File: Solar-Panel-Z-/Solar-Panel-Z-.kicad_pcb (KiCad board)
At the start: 6 copper layers, 48.4 x 48.4 mm, 73 parts, among them J1 FFC2B28-10-G, J2 U.FL-R-SMT-1, Q1 IRLML2803, U1 Value, U2 TSL2561, U3 NDS8434, U4 ATB2012-50011-T000

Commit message: Exported Gerbers
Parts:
- added H3: MountingHole, MountingHole:MountingHole_2.2mm_M2_DIN965, F.Cu at (84.0, 55.5)
- added H4: MountingHole, MountingHole:MountingHole_2.2mm_M2_DIN965, F.Cu at (84.0, 73.9)
- added H5: MountingHole, MountingHole:MountingHole_2.2mm_M2_DIN965, F.Cu at (123.8, 73.9)
- added H6: MountingHole, MountingHole:MountingHole_2.2mm_M2_DIN965, F.Cu at (123.8, 55.5)
- moved U2 0.97 mm to (112.4, 60.5)
- moved JP2 0.43 mm to (116.4, 53.7)
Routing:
- net /coil: track 13587.3 -> 13524.7 mm
- net GND: track 10.4 -> 9.34 mm, vias 1 -> 4
- net SDA1: track 30.1 -> 29.1 mm
- net SCL1: track 27.4 -> 26.4 mm
- net Net-(R1-Pad1): track 4.32 -> 3.37 mm
- net +3V3: track 59.0 -> 59.9 mm
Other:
- outline, holes or cut-outs redrawn

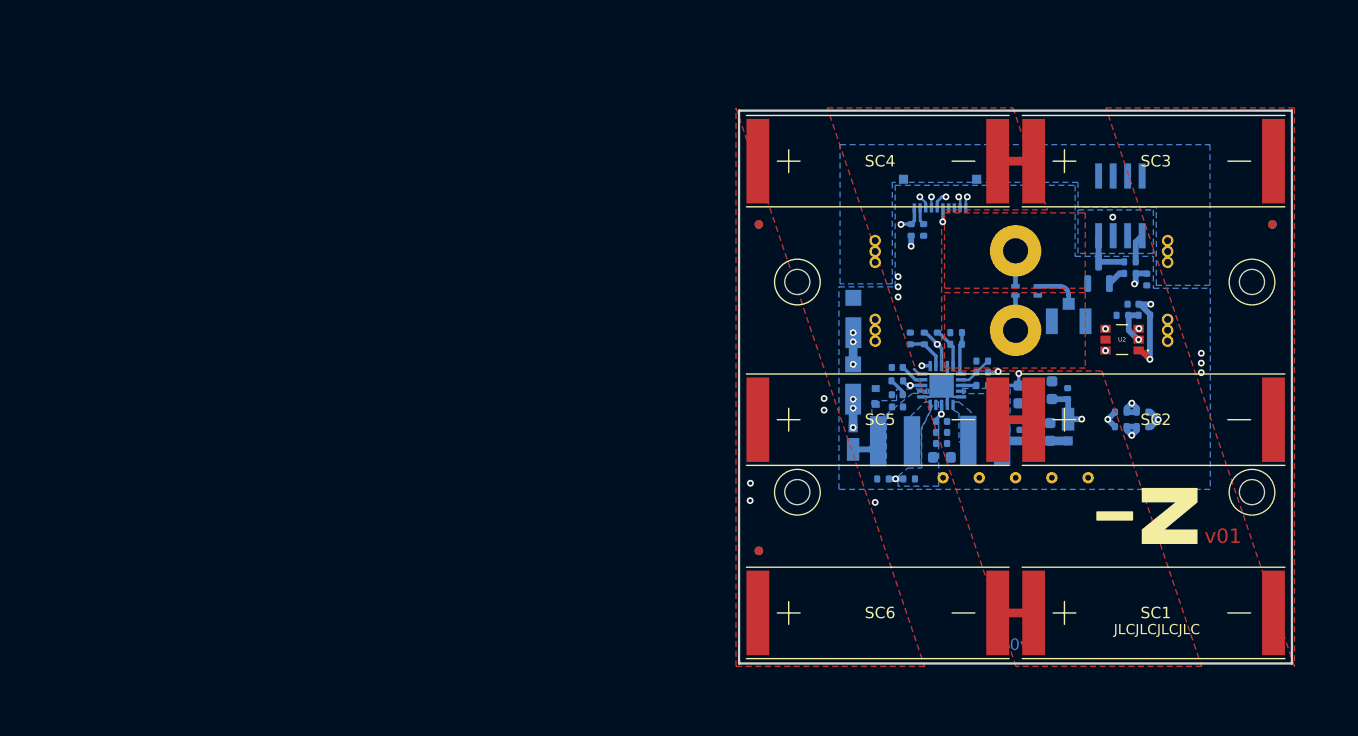
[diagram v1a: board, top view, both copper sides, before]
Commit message: Correct positions for everything except coils
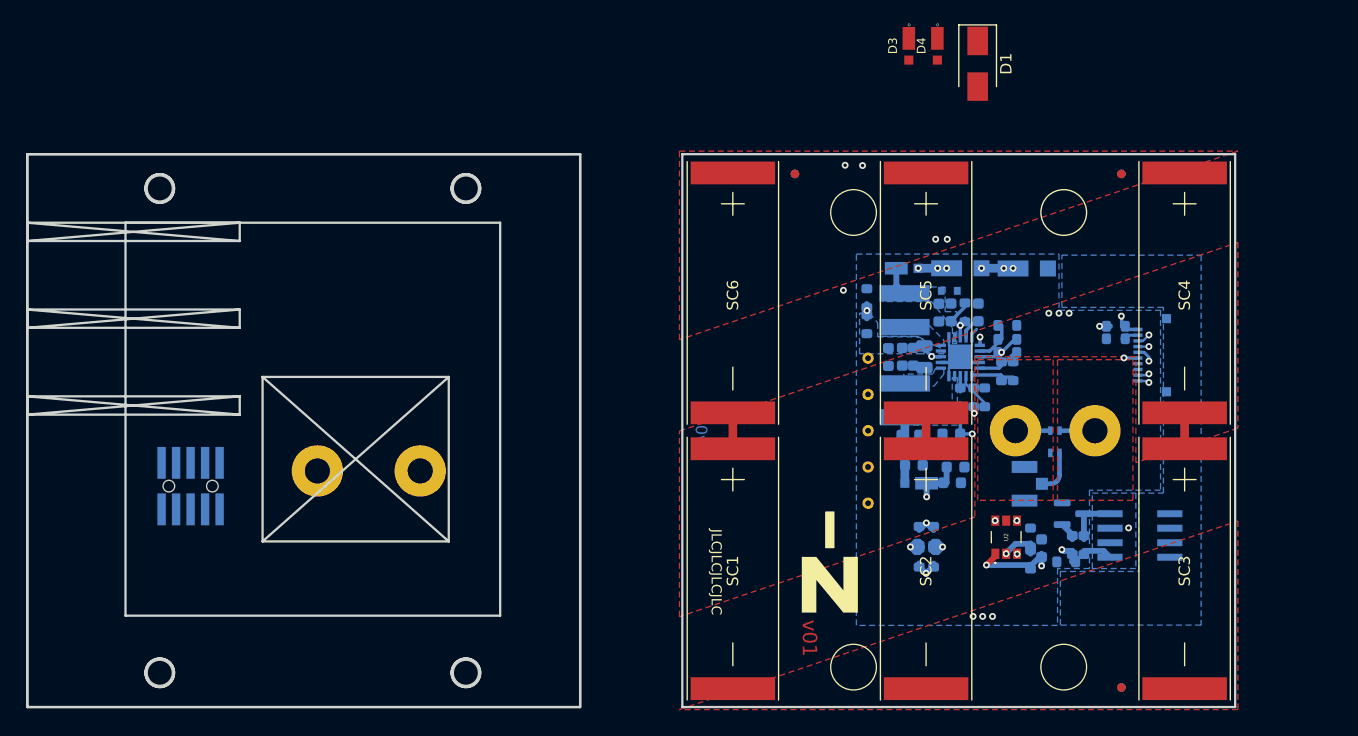
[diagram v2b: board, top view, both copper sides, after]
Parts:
- removed JP1, JP2: Jumper, solarpanels:Burn-Wire-Rotated
- added ?: , , F.Cu at (51.0, 72.0)
- added ?: , , F.Cu at (42.0, 72.0)
- added D1: SZ1SMA5918, Diode_SMD:D_SMA, F.Cu at (99.8, 36.4)
- added D3: MSS1P4-M3_89A, solarpanels:MICROSMP, F.Cu at (93.8, 34.8)
- added D4: MSS1P4-M3_89A, solarpanels:MICROSMP, F.Cu at (96.3, 34.8)
- added J1: TODO, batteryboard:FTS-105-XX-YY-DV-A, B.Cu at (30.9, 73.3)
- C1: value 1.0uF -> 1uF; footprint Capacitor_SMD:C_0402_1005Metric -> Capacitor_SMD:C_0603_1608Metric
- C10, C2, C3, C4, C9: footprint Capacitor_SMD:C_0402_1005Metric -> Capacitor_SMD:C_0603_1608Metric
- C11: renamed from C13; footprint Capacitor_SMD:C_0402_1005Metric -> Capacitor_SMD:C_0603_1608Metric
- C5: value 0.1uF -> 100uF; footprint Capacitor_SMD:C_0402_1005Metric -> Capacitor_SMD:C_0805_2012Metric
- C6: value 100uF -> 1uF
- C7: value 22uF -> 4.7uF; footprint Capacitor_SMD:C_0402_1005Metric -> Capacitor_SMD:C_0603_1608Metric
- C8: value 4.7uF -> 22uF; footprint Capacitor_SMD:C_0402_1005Metric -> Capacitor_SMD:C_0603_1608Metric
- R1, R10, R11, R12, R13, R14, R15, R16, R17, R18, R2, R5, R6, R7, R8, R9: footprint Resistor_SMD:R_0402_1005Metric -> Resistor_SMD:R_0603_1608Metric
- R19: renamed from R22; footprint Resistor_SMD:R_0402_1005Metric -> Resistor_SMD:R_0603_1608Metric
- R20: renamed from R3; footprint Resistor_SMD:R_0402_1005Metric -> Resistor_SMD:R_0603_1608Metric
- R21: renamed from R4; footprint Resistor_SMD:R_0402_1005Metric -> Resistor_SMD:R_0603_1608Metric
- R22: renamed from R19; footprint Resistor_SMD:R_0402_1005Metric -> Resistor_SMD:R_0603_1608Metric
- R3: renamed from R20; footprint Resistor_SMD:R_0402_1005Metric -> Resistor_SMD:R_0603_1608Metric
- R4: renamed from R21; footprint Resistor_SMD:R_0402_1005Metric -> Resistor_SMD:R_0603_1608Metric
- U1: value Value -> BQ25570RGRR
- moved H3 96.9 mm to (28.2, 89.7), turned to -90 degrees
- moved H4 76.9 mm to (55.0, 89.7), turned to -90 degrees
- moved H2 61.8 mm to (28.2, 47.3), turned to -90 degrees
- moved REF** 42.6 mm to (112.4, 91.0), turned to -90 degrees (x2)
- moved SC6 38.6 mm to (78.4, 45.9), turned to -90 degrees
- moved SC4 37.4 mm to (117.9, 45.9), turned to -90 degrees
- moved REF** 33.1 mm to (83.8, 46.0), turned to -90 degrees (x2)
- moved REF** 32.0 mm to (112.4, 46.0), turned to -90 degrees (x2)
- moved H1 30.1 mm to (55.0, 47.3), turned to -90 degrees
- moved SC1 30.0 mm to (78.4, 70.1), turned to -90 degrees
- moved Ref** 29.4 mm to (87.1, 81.3), turned to -90 degrees
- moved U3 28.9 mm to (114.0, 77.6), turned to 90 degrees
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- renumbered H3 to H1, H4 to H2, H5 to H3, H6 to H4, H1 to H5, H2 to H6
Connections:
- C7 pad 1: Net-(C11-Pad1) -> Net-(C7-Pad1)
- C9 pad 1: Net-(C11-Pad1) -> Net-(C7-Pad1)
- D5 pad 2: VSOLAR_FULL -> /VSOLAR_FULL
- R16 pad 1: Net-(C11-Pad1) -> Net-(C7-Pad1)
- SC4 pad 1: VSOLAR_FULL -> /VSOLAR_FULL
- SC5 pad 1: VSOLAR_FULL -> /VSOLAR_FULL
- SC6 pad 1: VSOLAR_FULL -> /VSOLAR_FULL
- TP1 pad 1: VSOLAR_FULL -> VSOLAR
- TP4 pad 1: BURN1 -> BATT_P
- TP5 pad 1: BATT_P -> BURN1
- U1 pad 19: Net-(C11-Pad1) -> Net-(C7-Pad1)
- U2 pad 4: SCL1 -> SCL3
- U2 pad 6: SDA1 -> SDA3
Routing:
- net BATT_P: track 49.9 -> 95.2 mm, vias 2 -> 4
- net BURN1: track 45.3 -> 0.00 mm, vias 2 -> 0
- net SCL1: track 26.4 -> 0.00 mm, vias 2 -> 0
- net SCL3: track 0.00 -> 26.4 mm, vias 0 -> 2
- net Net-(C7-Pad1): track 0.00 -> 18.4 mm, vias 0 -> 2
- net /VBAT: track 18.4 -> 0.00 mm, vias 2 -> 0
- net Net-(R10-Pad2): track 10.7 -> 17.7 mm
- net Net-(R5-Pad1): track 3.56 -> 0.00 mm
- net Net-(R7-Pad1): track 3.44 -> 0.00 mm
- net Net-(C4-Pad1): track 2.15 -> 0.00 mm
- net Net-(R14-Pad1): track 11.8 -> 14.0 mm
- net VBAT_OK: track 1.37 -> 0.00 mm
- net Net-(R10-Pad1): track 3.00 -> 4.37 mm
- net VSOLAR_FULL: vias 5 -> 3
- net VSOLAR: vias 0 -> 2
- added copper zone on F.Cu, net /VSOLAR_FULL
- added copper zone on B.Cu, net Net-(C7-Pad1)
- removed copper zone on B.Cu, net Net-(C11-Pad1)
- removed copper zone on F.Cu, net VSOLAR_FULL
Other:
- board size 48.4 x 48.4 mm -> 105.7 x 48.4 mm

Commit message: Retracing coils
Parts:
- removed the ? at (51.0, 72.0)
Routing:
- net /coil: track 13524.7 -> 14133.6 mm
- net (no net): track 0.00 -> 33.6 mm

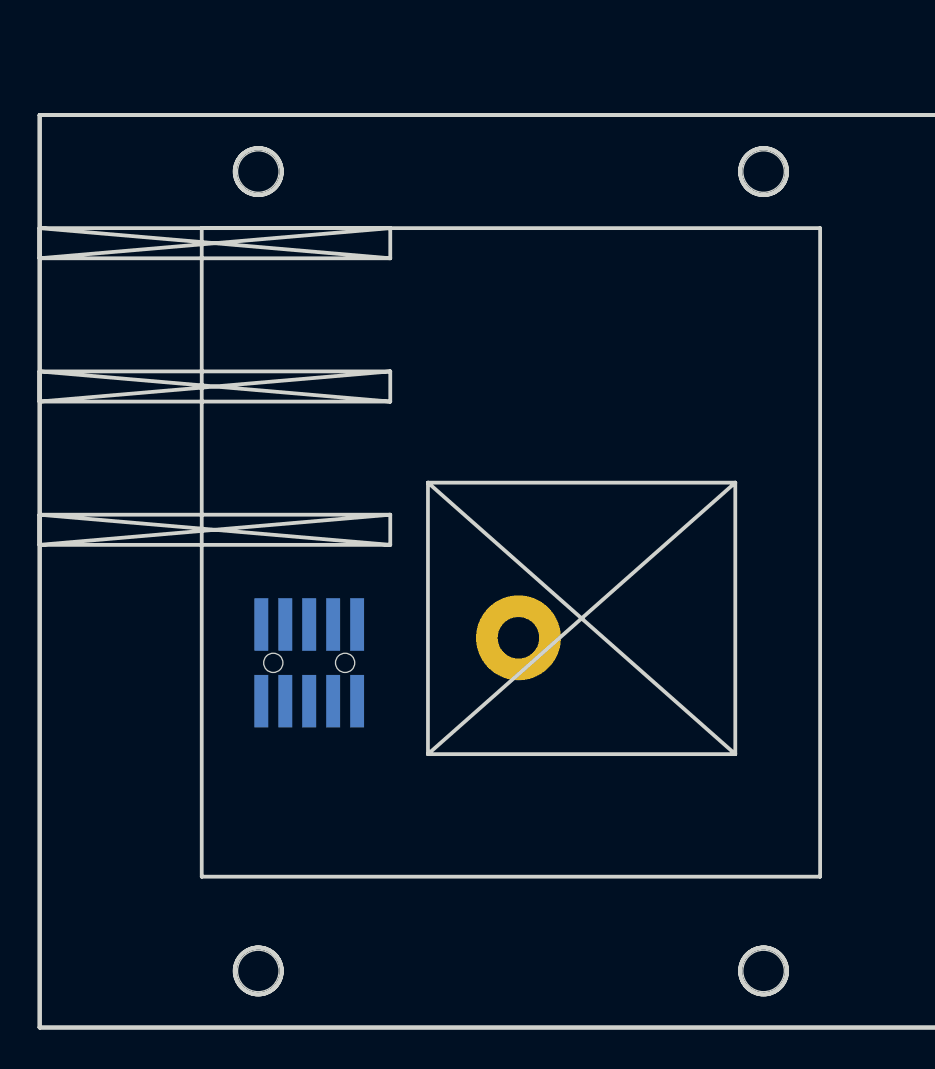
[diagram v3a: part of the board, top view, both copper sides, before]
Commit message: added 3d models to fix paths
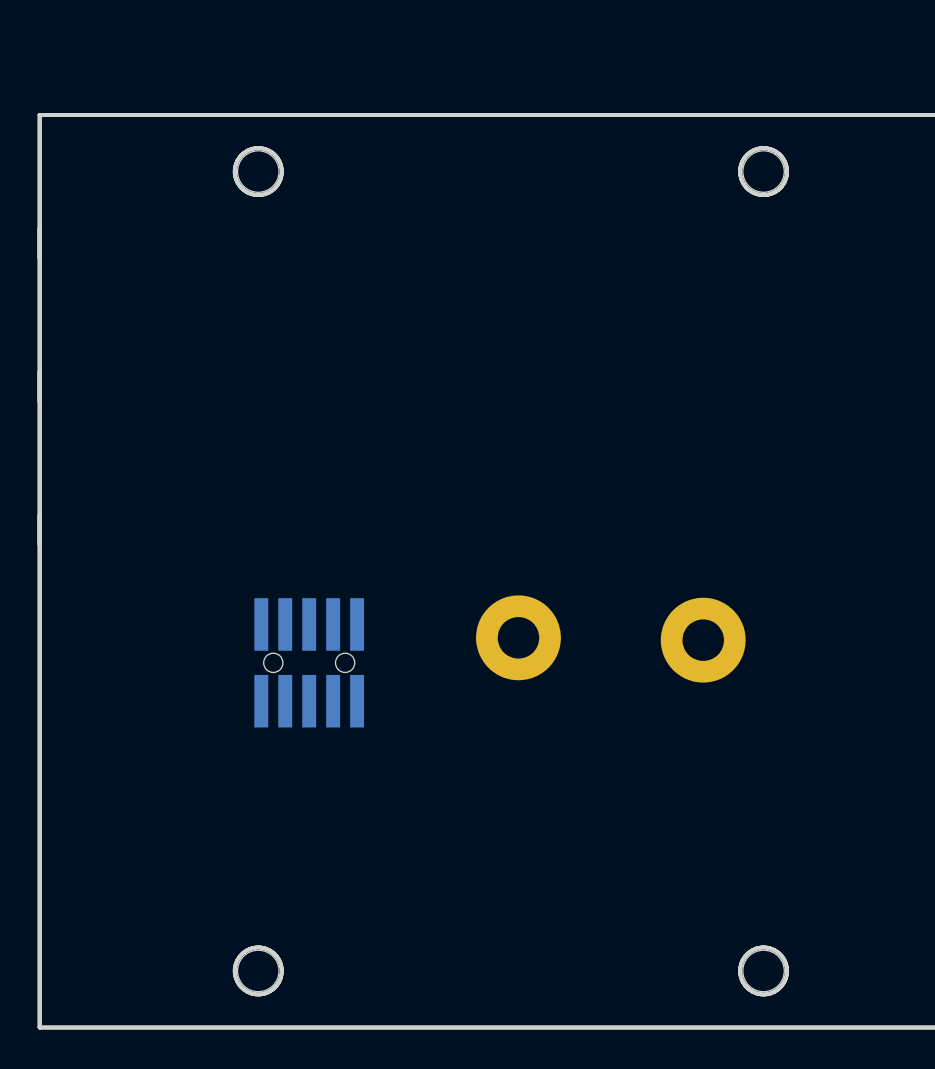
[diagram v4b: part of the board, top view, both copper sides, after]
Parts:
- added ?: , , F.Cu at (51.8, 72.1)
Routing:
- net /coil: track 14133.6 -> 14800.7 mm
- net (no net): track 33.6 -> 4.21 mm
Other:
- outline, holes or cut-outs redrawn

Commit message: copied over top layer pieces
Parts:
- removed the C11 at (97.6, 73.0)
- removed the C11 at (92.0, 62.0)
- removed the D1 at (99.8, 36.4)
- removed the D1 at (97.3, 56.2)
- removed the D3 at (93.8, 34.8)
- removed the D3 at (104.1, 54.3)
- removed the D4 at (96.3, 34.8)
- removed the D4 at (98.3, 54.3)
- removed the REF** at (112.4, 46.0) (x2)
- removed the REF** at (83.8, 46.0) (x2)
- removed the REF** at (112.4, 91.0) (x2)
- added ?: , , F.Cu at (20.7, 45.6)
- added ?: , , F.Cu at (39.4, 45.6)
- added ?: , , F.Cu at (20.9, 66.6)
- added ?: , , F.Cu at (61.0, 45.6)
- added ?: , , F.Cu at (20.9, 69.7)
- added C11: 100uF, Capacitor_SMD:C_0603_1608Metric, B.Cu at (100.1, 62.0)
- added C11: 0.1uF, Capacitor_SMD:C_0603_1608Metric, B.Cu at (105.7, 73.0)
- added D1: SZ1SMA5918, Diode_SMD:D_SMA, F.Cu at (107.9, 36.3)
- added D1: SDM20U40-7, Diode_SMD:D_SOD-523, B.Cu at (105.4, 56.2)
- added D3: MSS1P4-M3_89A, solarpanels:MICROSMP, F.Cu at (101.9, 34.7)
- added D3: SBDiode, solarpanels:SB Diode, B.Cu at (112.2, 54.2)
- added D4: MSS1P4-M3_89A, solarpanels:MICROSMP, F.Cu at (104.4, 34.7)
- added D4: SBDiode, solarpanels:SB Diode, B.Cu at (106.4, 54.2)
- added REF**: Fiducial_0.75mm_Mask1.5mm, Fiducial:Fiducial_0.75mm_Mask1.5mm, F.Cu at (120.5, 45.9)
- added REF**: Fiducial_0.75mm_Mask1.5mm, Fiducial:Fiducial_0.75mm_Mask1.5mm, F.Cu at (120.5, 90.9)
- added REF**: Fiducial_0.75mm_Mask1.5mm, Fiducial:Fiducial_0.75mm_Mask1.5mm, F.Cu at (91.9, 45.9)
- added REF**: Fiducial_0.75mm_Mask1.5mm, Fiducial:Fiducial_0.75mm_Mask1.5mm, B.Cu at (120.5, 45.9)
- added REF**: Fiducial_0.75mm_Mask1.5mm, Fiducial:Fiducial_0.75mm_Mask1.5mm, B.Cu at (91.9, 45.9)
- added REF**: Fiducial_0.75mm_Mask1.5mm, Fiducial:Fiducial_0.75mm_Mask1.5mm, B.Cu at (120.5, 90.9)
- moved C1 8.10 mm to (113.5, 78.7)
- moved C10 8.10 mm to (102.0, 70.0)
- moved C12 8.10 mm to (102.3, 71.4)
- moved C14 8.10 mm to (106.0, 71.6)
- moved C2 8.10 mm to (104.5, 58.1)
- moved C3 8.10 mm to (105.6, 58.1)
- moved C4 8.10 mm to (108.0, 58.1)
- moved C5 8.10 mm to (103.2, 61.9)
- moved C6 8.10 mm to (105.6, 68.7)
- moved C7 8.10 mm to (102.3, 61.9)
- moved C8 8.10 mm to (102.0, 68.8)
- moved C9 8.10 mm to (101.3, 61.9)
- moved D2 8.10 mm to (102.8, 73.0)
- moved D5 8.10 mm to (101.4, 54.2)
- moved H5 8.10 mm to (118.2, 68.4)
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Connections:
- C1 pad 1: GND -> (no net)
- C1 pad 2: +3V3 -> (no net)
- C10 pad 1: Net-(C10-Pad1) -> (no net)
- C10 pad 2: GND -> (no net)
- C12 pad 1: Net-(C10-Pad1) -> (no net)
- C12 pad 2: GND -> (no net)
- C14 pad 1: +3V3 -> (no net)
- C14 pad 2: GND -> (no net)
- C2 pad 1: VSOLAR -> (no net)
- C2 pad 2: GND -> (no net)
- C3 pad 1: VSOLAR -> (no net)
- C3 pad 2: GND -> (no net)
- C4 pad 1: Net-(C4-Pad1) -> (no net)
- C4 pad 2: GND -> (no net)
- C5 pad 1: /VBAT -> (no net)
- C5 pad 2: GND -> (no net)
- C6 pad 1: VOUT_EN -> (no net)
- C6 pad 2: GND -> (no net)
- C7 pad 1: Net-(C7-Pad1) -> (no net)
- C7 pad 2: GND -> (no net)
- C8 pad 1: Net-(C10-Pad1) -> (no net)
- C8 pad 2: GND -> (no net)
- C9 pad 1: Net-(C7-Pad1) -> (no net)
- C9 pad 2: GND -> (no net)
- D2 pad 1: +3V3 -> (no net)
- D2 pad 2: Net-(C10-Pad1) -> (no net)
- D5 pad 1: VSOLAR -> (no net)
- D5 pad 2: /VSOLAR_FULL -> (no net)
- J1 pad 1: BATT_P -> (no net)
- J1 pad 10: COIL_P -> (no net)
- J1 pad 2: BATT_N -> (no net)
- J1 pad 3: SDA1 -> (no net)
- J1 pad 4: SCL1 -> (no net)
- J1 pad 5: BURN1 -> (no net)
- J1 pad 6: +3V3 -> (no net)
- J1 pad 7: GND -> (no net)
- J1 pad 8: GND -> (no net)
- J1 pad 9: COIL_N -> (no net)
- J2 pad 1: GND -> (no net)
- J2 pad 2: GND -> (no net)
- J2 pad 3: Net-(J2-Pad3) -> (no net)
- L1 pad 1: VSOLAR -> (no net)
- L1 pad 2: Net-(L1-Pad2) -> (no net)
- L2 pad 1: Net-(L2-Pad1) -> (no net)
- L2 pad 2: Net-(C10-Pad1) -> (no net)
- Q1 pad 1: Net-(Q1-Pad1) -> (no net)
- Q1 pad 2: GND -> (no net)
- Q1 pad 3: Net-(Q1-Pad3) -> (no net)
- R1 pad 1: Net-(R1-Pad1) -> (no net)
- R1 pad 2: +3V3 -> (no net)
- R10 pad 1: Net-(R10-Pad1) -> (no net)
- R10 pad 2: Net-(R10-Pad2) -> (no net)
- R11 pad 1: GND -> (no net)
- R11 pad 2: Net-(R10-Pad1) -> (no net)
- R12 pad 1: COIL_P -> (no net)
- R13 pad 2: COIL_P -> (no net)
- R14 pad 1: Net-(R14-Pad1) -> (no net)
- R14 pad 2: VSOLAR -> (no net)
- R15 pad 1: GND -> (no net)
- R15 pad 2: Net-(R14-Pad1) -> (no net)
- R16 pad 1: Net-(C7-Pad1) -> (no net)
- R16 pad 2: Net-(R14-Pad1) -> (no net)
- R17 pad 1: COIL_N -> (no net)
- R18 pad 2: COIL_N -> (no net)
- R19 pad 1: VBAT_OK -> (no net)
- R19 pad 2: VOUT_EN -> (no net)
- R2 pad 1: GND -> (no net)
- R2 pad 2: Net-(R1-Pad1) -> (no net)
- R20 pad 1: BURN1 -> (no net)
- R20 pad 2: GND -> (no net)
- R21 pad 1: Net-(Q1-Pad1) -> (no net)
- R21 pad 2: BURN1 -> (no net)
- R22 pad 1: Net-(Q1-Pad3) -> (no net)
- R22 pad 2: BATT_P -> (no net)
- R3 pad 1: BATT_P -> (no net)
- R3 pad 2: /VBAT -> (no net)
- R4 pad 1: BATT_N -> (no net)
- R4 pad 2: GND -> (no net)
- R5 pad 1: Net-(R5-Pad1) -> (no net)
- R5 pad 2: Net-(R10-Pad2) -> (no net)
- R6 pad 1: GND -> (no net)
- R6 pad 2: Net-(R5-Pad1) -> (no net)
- R7 pad 1: Net-(R7-Pad1) -> (no net)
- R7 pad 2: Net-(R10-Pad2) -> (no net)
- R8 pad 1: Net-(R8-Pad1) -> (no net)
- R8 pad 2: Net-(R7-Pad1) -> (no net)
- R9 pad 1: GND -> (no net)
- R9 pad 2: Net-(R8-Pad1) -> (no net)
- SC1 pad 1: Net-(D3-Pad1) -> (no net)
- SC1 pad 2: GND -> (no net)
- SC2 pad 1: Net-(D3-Pad1) -> (no net)
- SC2 pad 2: GND -> (no net)
- SC3 pad 1: Net-(D3-Pad1) -> (no net)
- SC3 pad 2: GND -> (no net)
- SC4 pad 1: /VSOLAR_FULL -> (no net)
- SC4 pad 2: Net-(D3-Pad1) -> (no net)
- SC5 pad 1: /VSOLAR_FULL -> (no net)
- SC5 pad 2: Net-(D3-Pad1) -> (no net)
- SC6 pad 1: /VSOLAR_FULL -> (no net)
- SC6 pad 2: Net-(D3-Pad1) -> (no net)
- TP1 pad 1: VSOLAR -> (no net)
- TP2 pad 1: GND -> (no net)
- TP3 pad 1: +3V3 -> (no net)
- TP4 pad 1: BATT_P -> (no net)
- TP5 pad 1: BURN1 -> (no net)
- U1 pad 1: GND -> (no net)
- U1 pad 10: Net-(R7-Pad1) -> (no net)
- U1 pad 11: Net-(R8-Pad1) -> (no net)
- U1 pad 12: Net-(R10-Pad1) -> (no net)
- U1 pad 13: VBAT_OK -> (no net)
- U1 pad 14: Net-(C10-Pad1) -> (no net)
- U1 pad 15: GND -> (no net)
- U1 pad 16: Net-(L2-Pad1) -> (no net)
- U1 pad 17: GND -> (no net)
- U1 pad 18: /VBAT -> (no net)
- U1 pad 19: Net-(C7-Pad1) -> (no net)
- U1 pad 2: VSOLAR -> (no net)
- U1 pad 20: Net-(L1-Pad2) -> (no net)
- U1 pad 21: GND -> (no net)
- U1 pad 3: Net-(R14-Pad1) -> (no net)
- U1 pad 4: Net-(C4-Pad1) -> (no net)
- U1 pad 5: GND -> (no net)
- U1 pad 6: VOUT_EN -> (no net)
- U1 pad 7: Net-(R5-Pad1) -> (no net)
- U1 pad 8: Net-(R10-Pad2) -> (no net)
- U1 pad 9: GND -> (no net)
- U2 pad 1: +3V3 -> (no net)
- U2 pad 2: Net-(R1-Pad1) -> (no net)
- U2 pad 3: GND -> (no net)
- U2 pad 4: SCL3 -> (no net)
- U2 pad 5: unconnected-(U2-Pad5) -> (no net)
- U2 pad 6: SDA3 -> (no net)
- U3 pad 1: BATT_P -> (no net)
- U3 pad 2: BATT_P -> (no net)
- U3 pad 3: BATT_P -> (no net)
- U3 pad 4: Net-(Q1-Pad3) -> (no net)
- U3 pad 5: /VBURN -> (no net)
- U3 pad 6: /VBURN -> (no net)
- U3 pad 7: /VBURN -> (no net)
- U3 pad 8: /VBURN -> (no net)
- U4 pad 1: Net-(J2-Pad3) -> (no net)
- U4 pad 2: GND -> (no net)
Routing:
- net (no net): track 4.21 -> 440.2 mm, vias 0 -> 40
- net BATT_P: track 95.2 -> 0.00 mm, vias 4 -> 0
- net +3V3: track 59.9 -> 0.00 mm, vias 4 -> 0
- net COIL_N: track 37.6 -> 0.00 mm, vias 2 -> 0
- net COIL_P: track 35.1 -> 0.00 mm, vias 2 -> 0
- net SDA1: track 29.1 -> 0.00 mm, vias 2 -> 0
- net SCL3: track 26.4 -> 0.00 mm, vias 2 -> 0
- net Net-(D3-Pad1): track 22.4 -> 0.00 mm, vias 6 -> 0
- net VSOLAR_FULL: track 20.6 -> 0.00 mm, vias 3 -> 0
- net Net-(C7-Pad1): track 18.4 -> 0.00 mm, vias 2 -> 0
- net Net-(R10-Pad2): track 17.7 -> 0.00 mm, vias 2 -> 0
- net VOUT_EN: track 14.2 -> 0.00 mm, vias 2 -> 0
- net Net-(R14-Pad1): track 14.0 -> 0.00 mm, vias 2 -> 0
- net GND: track 9.34 -> 0.00 mm, vias 4 -> 0
- net Net-(C10-Pad1): track 5.77 -> 0.00 mm
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- added copper zone on B.Cu, net (none)
- added copper zone on F.Cu, net (none)
- removed copper zone on B.Cu, net /VBURN
- removed copper zone on F.Cu, net /VSOLAR_FULL
- removed copper zone on B.Cu, net BATT_P
- removed copper zone on B.Cu, net GND
- removed copper zone on F.Cu, net GND
- removed copper zone on B.Cu, net Net-(C10-Pad1)
- removed copper zone on B.Cu, net Net-(C7-Pad1)
- removed copper zone on F.Cu, net Net-(D3-Pad1)
- removed copper zone on B.Cu, net Net-(L1-Pad2)
- removed copper zone on B.Cu, net Net-(L2-Pad1)
- removed copper zone on B.Cu, net VSOLAR
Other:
- board size 105.7 x 48.4 mm -> 113.8 x 48.5 mm
